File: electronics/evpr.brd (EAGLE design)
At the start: 97.2 x 41.3 mm, 115 parts, among them J1 10118193-0001LF, Q1 AOD4184A, Q2 AOD4184A, T3 MMBT2222A, T5 MMBT2222A, U1 BQ2057TTS, U3 ESP32-WROOM-32D, U6 SN74AHCT125DR, U7 TPSM84824MOLR, U8 LTC4353CMSPBFMSOP-16_MS-M, X1 B3P-VH(LF)(SN), X2 BM02B-PASS-1-TFT(LF)(SN), X3 BM03B-PASS-1-TFT(LF)(SN), X4 BM03B-PASS-1-TFT(LF)(SN), X5 BM04B-PASS-1-TFT(LF)(SN)

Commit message: Updated all DPAK components to use single package with detailed tkeepout
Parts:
- Q1, Q2: device mccloud:DPAK228P994X240-4N -> mccloud:DPACK
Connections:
- net SYS_POWER: now also Q1.2, Q2.2; no longer Q1.4, Q2.4
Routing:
- net VBAT: track 86.8 -> 89.8 mm
- net N$10: track 8.41 -> 9.12 mm
- net N$4: track 7.31 -> 6.60 mm
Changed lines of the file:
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@@
 <layer number="37" name="tTest" color="7" fill="1" visible="no" active="yes"/>
 <layer number="38" name="bTest" color="7" fill="1" visible="no" active="yes"/>
-<layer number="39" name="tKeepout" color="4" fill="11" visible="no" active="yes"/>
-<layer number="40" name="bKeepout" color="1" fill="11" visible="no" active="yes"/>
+<layer number="39" name="tKeepout" color="4" fill="11" visible="yes" active="yes"/>
+<layer number="40" name="bKeepout" color="1" fill="11" visible="yes" active="yes"/>
 <layer number="41" name="tRestrict" color="4" fill="10" visible="no" active="yes"/>
 <layer number="42" name="bRestrict" color="1" fill="10" visible="no" active="yes"/>
@@
 <attribute name="VALUE" x="-13.1826" y="-44.703996875" size="1.27" layer="28" rot="MR0"/>
 </element>
-<element name="Q1" library="mccloud" package="DPAK228P994X240-4N" value="AOD4184A" x="-7.239" y="-38.354" smashed="yes" rot="MR90">
+<element name="Q1" library="mccloud" package="DPACK" value="AOD4184A" x="-7.239" y="-38.354" smashed="yes" rot="MR90">
 <attribute name="COMPONENT" value="AOD4184A" x="-7.239" y="-38.354" size="1.778" layer="28" rot="MR90" display="off"/>
-<attribute name="DESCRIPTION" value=" Trans MOSFET N-CH 40V 50A 3-Pin_2+Tab_ DPAK " x="-7.239" y="-38.354" size="1.778" layer="28" rot="MR90" display="off"/>
-<attribute name="DIGI-KEY_PART_NUMBER" value="785-1221-1-ND" x="-7.239" y="-38.354" size="1.778" layer="28" rot="MR90" display="off"/>
-<attribute name="DIGI-KEY_PURCHASE_URL" value="https://www.digikey.com/product-detail/en/alpha-omega-semiconductor-inc/AOD4184A/785-1221-1-ND/2353939?utm_source=snapeda&amp;utm_medium=aggregator&amp;utm_campaign=symbol" x="-7.239" y="-38.354" size="1.778" layer="28" rot="MR90" display="off"/>
-<attribute name="MF" value="Alpha &amp;" x="-7.239" y="-38.354" size="1.778" layer="28" rot="MR90" display="off"/>
-<attribute name="MP" value="AOD4184A" x="-7.239" y="-38.354" size="1.778" layer="28" rot="MR90" display="off"/>
 <attribute name="NAME" x="-0.981559375" y="-42.06078125" size="1.27233125" layer="26" ratio="10" rot="MR90"/>
-<attribute name="PACKAGE" value="TO-252 Alpha &amp;amp; Omega Semiconductor" x="-7.239" y="-38.354" size="1.778" layer="28" rot="MR90" display="off"/>
 <attribute name="VALUE" x="-15.0058" y="-42.3606" size="1.2721" layer="28" ratio="10" rot="MR90"/>
 </element>
-<element name="Q2" library="mccloud" package="DPAK228P994X240-4N" value="AOD4184A" x="-19.812" y="-50.546" smashed="yes" rot="MR270">
+<element name="Q2" library="mccloud" package="DPACK" value="AOD4184A" x="-19.812" y="-50.546" smashed="yes" rot="MR270">
 <attribute name="COMPONENT" value="AOD4184A" x="-19.812" y="-50.546" size="1.778" layer="28" rot="MR270" display="off"/>
-<attribute name="DESCRIPTION" value=" Trans MOSFET N-CH 40V 50A 3-Pin_2+Tab_ DPAK " x="-19.812" y="-50.546" size="1.778" layer="28" rot="MR270" display="off"/>
-<attribute name="DIGI-KEY_PART_NUMBER" value="785-1221-1-ND" x="-19.812" y="-50.546" size="1.778" layer="28" rot="MR270" display="off"/>
-<attribute name="DIGI-KEY_PURCHASE_URL" value="https://www.digikey.com/product-detail/en/alpha-omega-semiconductor-inc/AOD4184A/785-1221-1-ND/2353939?utm_source=snapeda&amp;utm_medium=aggregator&amp;utm_campaign=symbol" x="-19.812" y="-50.546" size="1.778" layer="28" rot="MR270" display="off"/>
-<attribute name="MF" value="Alpha &amp;" x="-19.812" y="-50.546" size="1.778" layer="28" rot="MR270" display="off"/>
-<attribute name="MP" value="AOD4184A" x="-19.812" y="-50.546" size="1.778" layer="28" rot="MR270" display="off"/>
 <attribute name="NAME" x="-26.069440625" y="-46.83921875" size="1.27233125" layer="26" ratio="10" rot="MR270"/>
-<attribute name="PACKAGE" value="TO-252 Alpha &amp;amp; Omega Semiconductor" x="-19.812" y="-50.546" size="1.778" layer="28" rot="MR270" display="off"/>
 <attribute name="VALUE" x="-12.0452" y="-46.5394" size="1.2721" layer="28" ratio="10" rot="MR270"/>
 </element>
@@
 <wire x1="-12.446" y1="-36.068" x2="-12.319" y2="-35.941" width="1.016" layer="16"/>
 <wire x1="-12.319" y1="-35.941" x2="-11.456" y2="-35.941" width="1.016" layer="16"/>
-<wire x1="-11.456" y1="-35.941" x2="-11.329" y2="-36.068" width="1.016" layer="16"/>
+<wire x1="-11.456" y1="-35.941" x2="-12.039" y2="-36.074" width="1.016" layer="16"/>
 <wire x1="-11.456" y1="-37.618" x2="-11.456" y2="-35.941" width="1.016" layer="16"/>
 <wire x1="-14.478" y1="-40.64" x2="-11.456" y2="-37.618" width="1.016" layer="16"/>
@@
 <via x="-15.621" y="-53.975" extent="1-16" drill="0.6096"/>
 <wire x1="-15.621" y1="-53.975" x2="-15.621" y2="-52.933" width="1.016" layer="16"/>
-<wire x1="-15.621" y1="-52.933" x2="-15.722" y2="-52.832" width="1.016" layer="16"/>
+<wire x1="-15.621" y1="-52.933" x2="-15.012" y2="-52.826" width="1.016" layer="16"/>
 <wire x1="-16.637" y1="-53.975" x2="-16.637" y2="-53.747" width="1.016" layer="16"/>
-<wire x1="-16.637" y1="-53.747" x2="-15.722" y2="-52.832" width="1.016" layer="16"/>
-<wire x1="-15.722" y1="-52.832" x2="-17.526" y2="-52.832" width="1.016" layer="16"/>
+<wire x1="-16.637" y1="-53.747" x2="-15.012" y2="-52.826" width="1.016" layer="16"/>
+<wire x1="-15.012" y1="-52.826" x2="-17.526" y2="-52.832" width="1.016" layer="16"/>
 <wire x1="-17.526" y1="-52.832" x2="-18.6565" y2="-53.9625" width="1.016" layer="16"/>
 <wire x1="-18.6565" y1="-53.9625" x2="-18.669" y2="-53.9625" width="1.016" layer="16"/>
@@
 <wire x1="-17.78" y1="-53.9625" x2="-16.8525" y2="-53.9625" width="1.016" layer="16"/>
 <wire x1="-16.8525" y1="-53.9625" x2="-15.6335" y2="-53.9625" width="1.016" layer="16"/>
-<wire x1="-15.722" y1="-52.832" x2="-16.8525" y2="-53.9625" width="1.016" layer="16"/>
-<wire x1="-15.722" y1="-52.832" x2="-16.6495" y2="-52.832" width="1.016" layer="16"/>
+<wire x1="-15.012" y1="-52.826" x2="-16.8525" y2="-53.9625" width="1.016" layer="16"/>
+<wire x1="-15.012" y1="-52.826" x2="-16.6495" y2="-52.832" width="1.016" layer="16"/>
 <wire x1="-16.6495" y1="-52.832" x2="-17.78" y2="-53.9625" width="1.016" layer="16"/>
 <wire x1="-15.621" y1="-53.975" x2="-16.637" y2="-53.975" width="1.016" layer="1"/>
@@
 <vertex x="35.052" y="-43.18"/>
 </polygon>
-<contactref element="Q1" pad="4"/>
-<contactref element="Q2" pad="4"/>
+<contactref element="Q1" pad="2"/>
+<contactref element="Q2" pad="2"/>
 <contactref element="U8" pad="7"/>
 <via x="-0.9144" y="-36.4236" extent="1-16" drill="0.6096"/>
@@
 <contactref element="X4" pad="P$1"/>
 <contactref element="X3" pad="P$1"/>
-<wire x1="-70.326" y1="-253.786" x2="56.166" y2="-41.696" width="0" layer="19" extent="1-1"/>
-<wire x1="-67.326" y1="-242.61" x2="-70.326" y2="-253.786" width="0" layer="19" extent="1-1"/>
-<wire x1="-61.126" y1="-206.248" x2="-67.326" y2="-242.61" width="0" layer="19" extent="1-1"/>
-<wire x1="-24.511" y1="-53.975" x2="-61.126" y2="-206.248" width="0" layer="19" extent="1-1"/>
 <wire x1="-23.622" y1="-51.816" x2="-24.384" y2="-52.07" width="0" layer="19" extent="16-16"/>
 <wire x1="-22.479" y1="-53.975" x2="-23.495" y2="-53.975" width="0" layer="19" extent="1-1"/>
 <wire x1="-21.844" y1="-52.07" x2="-22.606" y2="-52.324" width="0" layer="19" extent="16-16"/>
 <wire x1="-20.447" y1="-53.975" x2="-21.463" y2="-53.975" width="0" layer="19" extent="1-1"/>
-<wire x1="-22.252" y1="-50.546" x2="-21.844" y2="-52.07" width="0" layer="19" extent="16-16"/>
+<wire x1="-22.312" y1="-50.546" x2="-21.844" y2="-52.07" width="0" layer="19" extent="16-16"/>
 <wire x1="-10.3378" y1="-46.10735" x2="-20.574" y2="-52.324" width="0" layer="19" extent="16-16"/>
 <wire x1="-5.8674" y1="-46.10735" x2="-8.703328125" y2="-47.176671875" width="0" layer="19" extent="2-16"/>
@@
 <wire x1="-3.6068" y1="-41.91" x2="-6.7564" y2="-41.783" width="0" layer="19" extent="1-2"/>
 <wire x1="-2.7178" y1="-41.8338" x2="-3.6068" y2="-41.91" width="0" layer="19" extent="1-2"/>
-<wire x1="-4.799" y1="-38.354" x2="-3.683" y2="-40.513" width="0" layer="19" extent="2-16"/>
-<wire x1="-3.048" y1="-37.592" x2="-4.799" y2="-38.354" width="0" layer="19" extent="16-16"/>
+<wire x1="-4.739" y1="-38.354" x2="-3.683" y2="-40.513" width="0" layer="19" extent="2-16"/>
+<wire x1="-3.048" y1="-37.592" x2="-4.739" y2="-38.354" width="0" layer="19" extent="16-16"/>
 <wire x1="-0.9144" y1="-36.4236" x2="-0.9144" y2="-37.6936" width="0" layer="19" extent="1-1"/>
 <wire x1="-4.572" y1="-36.322" x2="-3.048" y2="-37.592" width="0" layer="19" extent="16-16"/>
@@
 <wire x1="21.779" y1="-31.9091625" x2="-0.9144" y2="-36.4236" width="0" layer="19" extent="1-1"/>
 <wire x1="33.975" y1="-30.196" x2="24.0284" y2="-31.496" width="0" layer="19" extent="1-1"/>
+<wire x1="56.166" y1="-41.696" x2="35.5982" y2="-31.7542" width="0" layer="19" extent="1-1"/>
+<wire x1="-61.126" y1="-206.248" x2="-24.511" y2="-53.975" width="0" layer="19" extent="1-1"/>
+<wire x1="-67.326" y1="-242.61" x2="-61.126" y2="-206.248" width="0" layer="19" extent="1-1"/>
+<wire x1="-70.326" y1="-253.786" x2="-67.326" y2="-242.61" width="0" layer="19" extent="1-1"/>
 </signal>
 <signal name="SHUTDOWN">
@@
 <contactref element="U8" pad="12"/>
 <contactref element="Q2" pad="1"/>
-<wire x1="-15.722" y1="-48.26" x2="-13.7414" y2="-48.26" width="0.254" layer="16"/>
+<wire x1="-15.012" y1="-48.266" x2="-13.7414" y2="-48.26" width="0.254" layer="16"/>
 <wire x1="-13.7414" y1="-48.26" x2="-13.716" y2="-48.2854" width="0.254" layer="16"/>
 <via x="-13.716" y="-48.2854" extent="1-16" drill="0.254"/>
@@
 <via x="-8.89" y="-41.402" extent="1-16" drill="0.254"/>
 <wire x1="-8.89" y1="-41.402" x2="-9.652" y2="-40.64" width="0.254" layer="16"/>
-<wire x1="-9.652" y1="-40.64" x2="-11.329" y2="-40.64" width="0.254" layer="16"/>
+<wire x1="-9.652" y1="-40.64" x2="-12.039" y2="-40.634" width="0.254" layer="16"/>
 <wire x1="-7.066071875" y1="-45.106590625" x2="-8.4582" y2="-43.7144625" width="0.254" layer="16"/>
 </signal>

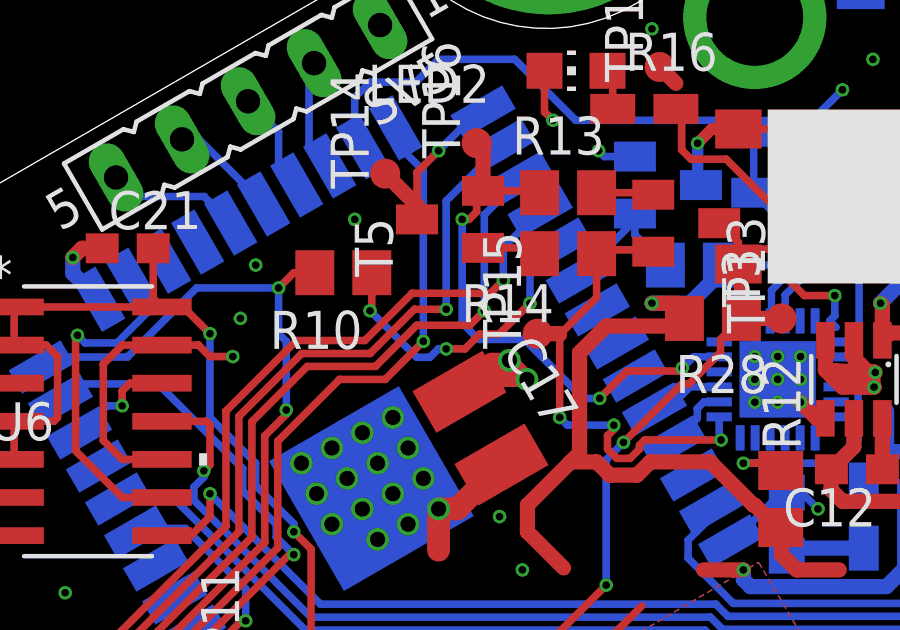
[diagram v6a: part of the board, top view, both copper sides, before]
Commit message: Rerouted CSTAT pins
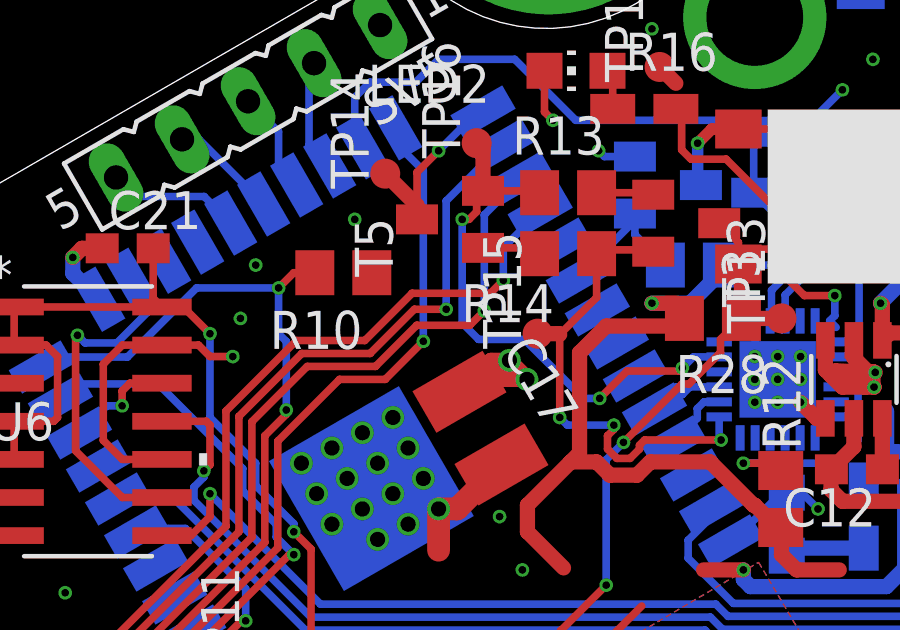
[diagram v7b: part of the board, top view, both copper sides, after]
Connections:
- removed net N$47: R10.1
- new net N$2: R10.1, U3.31
- net CSTAT: now also U3.36
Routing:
- net N$47: track 9.02 -> 0.00 mm, vias 3 -> 0
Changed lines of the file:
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@@
 <wire x1="15.2908" y1="-36.9305375" x2="15.2908" y2="-33.3745375" width="0.254" layer="1"/>
 <contactref element="U1" pad="5"/>
+<contactref element="U3" pad="36"/>
 <wire x1="-6.817" y1="-51.267" x2="-56.312" y2="-239.735" width="0" layer="19" extent="1-1"/>
+<wire x1="29.54921875" y1="-34.6815875" x2="16.005828125" y2="-32.515828125" width="0" layer="19" extent="16-16"/>
 </signal>
 <signal name="N$8">
@@
 <wire x1="27.6274" y1="-26.6724" x2="28.641" y2="-27.686" width="0.254" layer="16"/>
 </signal>
-<signal name="N$47">
-<contactref element="R10" pad="1"/>
-<wire x1="24.13" y1="-27.956840625" x2="24.13" y2="-28.956" width="0.254" layer="16"/>
-<via x="24.13" y="-28.956" extent="1-16" drill="0.254"/>
-<via x="21.336" y="-30.48" extent="1-16" drill="0.254"/>
-<wire x1="21.961775" y1="-30.48" x2="21.336" y2="-30.48" width="0.254" layer="1"/>
-<wire x1="24.13" y1="-28.956" x2="23.100346875" y2="-29.985653125" width="0.254" layer="1"/>
-<wire x1="23.100346875" y1="-29.985653125" x2="22.456121875" y2="-29.985653125" width="0.254" layer="1"/>
-<wire x1="22.456121875" y1="-29.985653125" x2="21.961775" y2="-30.48" width="0.254" layer="1"/>
-<via x="18.796" y="-29.21" extent="1-16" drill="0.254"/>
-<wire x1="20.79494375" y1="-30.7594" x2="20.35305625" y2="-30.7594" width="0.254" layer="16"/>
-<wire x1="21.336" y1="-30.48" x2="21.07434375" y2="-30.48" width="0.254" layer="16"/>
-<wire x1="21.07434375" y1="-30.48" x2="20.79494375" y2="-30.7594" width="0.254" layer="16"/>
-<wire x1="18.80365625" y1="-29.21" x2="18.796" y2="-29.21" width="0.254" layer="16"/>
-<wire x1="20.35305625" y1="-30.7594" x2="18.80365625" y2="-29.21" width="0.254" layer="16"/>
-<wire x1="18.796" y1="-29.21" x2="18.857" y2="-29.149" width="0.254" layer="1"/>
-<wire x1="18.857" y1="-29.149" x2="18.857" y2="-27.94" width="0.254" layer="1"/>
-</signal>
 <signal name="N$49">
 <contactref element="U3" pad="19"/>
@@
 <wire x1="-56.312" y1="-238.435" x2="-10.6324" y2="-53.1368" width="0" layer="19" extent="1-1"/>
 </signal>
+<signal name="N$2">
+<contactref element="U3" pad="31"/>
+<contactref element="R10" pad="1"/>
+<wire x1="26.37421875" y1="-29.182325" x2="18.857" y2="-27.94" width="0" layer="19" extent="1-16"/>
+</signal>
 </signals>

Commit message: Replace passives with 0603 wherever possible.
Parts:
- added C27, C28, C29, C30, C31, C32, C33, C34, C35, C36, C37, C38: 0.1uF, eagle-ltspice:C0603
- C14, C15, C17, C19, C20: device eagle-ltspice:C1210 -> rcl:C0603
- R1, R10, R12, R13, R14, R28, R32, R33, R34, R4, R5, R6, R7, R9: device rcl:R0805 -> rcl:R0603
- R11: value 768Ω 1% -> 768Ω 0.1%
- R15, R16, R17, R18, R19, R20, R21, R22, R23, R24, R25, R26, R27, R30: device rcl:R0805W -> rcl:R0603
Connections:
- net 5.0V: now also C36.2
- net ESP_POWER: now also C34.2
- net GND: now also C27.2, C28.2, C29.1, C30.2, C31.2, C32.2, C33.2, C34.1, C35.1, C36.1, C37.1, C38.1
- net N$51: now also C35.2
- net N$8: now also C31.1
- net SYS_POWER: now also C33.1, C37.2, C38.2
- net TACH_RAW: now also C27.1
- net VBAT: now also C30.1, C32.1
- net VCONV: now also C29.2
- net VRAW: now also C28.1
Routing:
- net VBAT: track 89.8 -> 86.3 mm
- net N$51: track 7.90 -> 9.67 mm
- net GND: track 83.2 -> 84.6 mm
- net SYS_POWER: track 41.9 -> 42.4 mm
